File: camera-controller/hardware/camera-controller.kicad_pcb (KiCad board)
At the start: 4 copper layers, 40 x 40 mm, 69 parts, among them J2 Conn_Coaxial, J3 Conn_01x04, J4 Conn_01x08, J5 Micro_SD_Card_Det1, J6 Conn_01x02, U1 STM32H523RCTx, U2 LR2021, Y1 32.768MHz, Y2 24MHz, Y3 32MHz 10pF

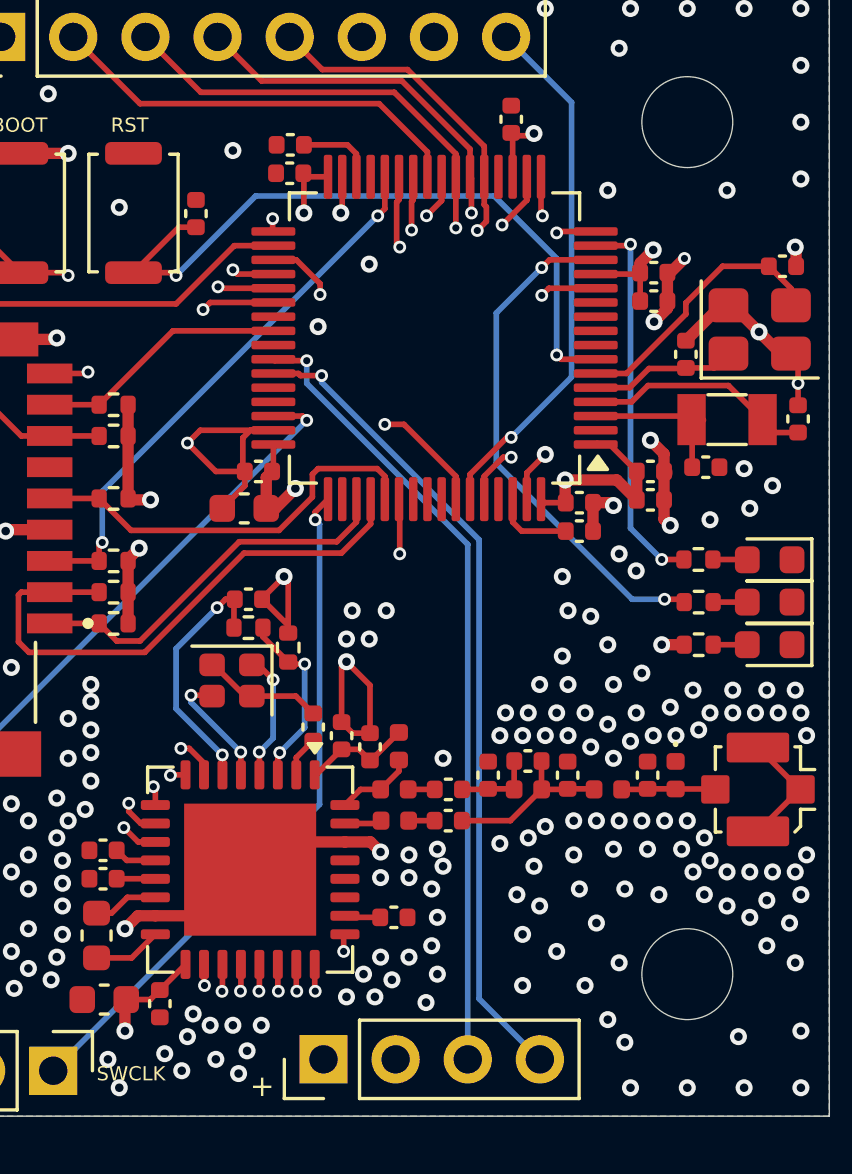
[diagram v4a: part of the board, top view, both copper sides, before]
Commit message: optimized power trace
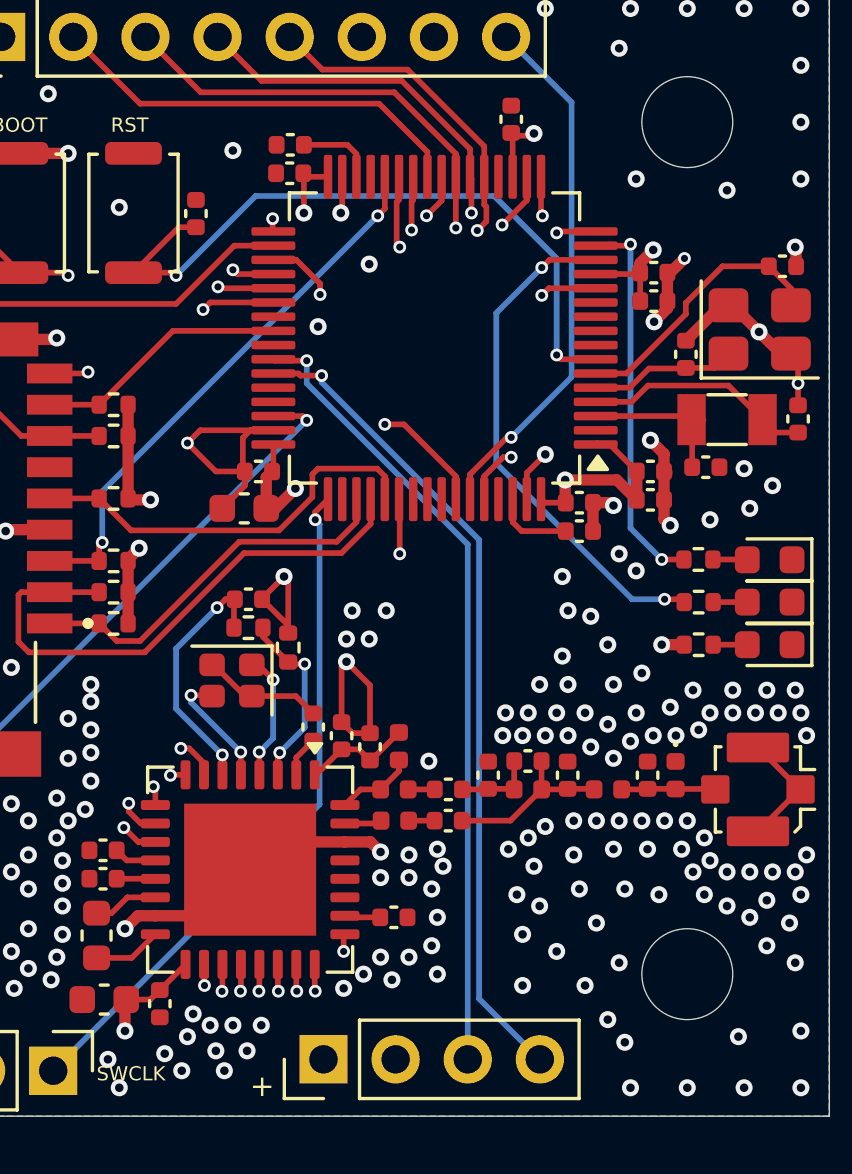
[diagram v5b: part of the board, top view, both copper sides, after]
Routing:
- net +3.3V: track 44.6 -> 69.9 mm
- net GND: vias 232 -> 230
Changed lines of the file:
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@@
 	)
 	(segment
-		(start 125.2 107.38995)
-		(end 127.01005 109.2)
-		(width 0.4)
+		(start 137.7 90.6)
+		(end 140.7 87.6)
+		(width 0.6)
 		(layer "In1.Cu")
 		(net "+3.3V")
 	)
 	(segment
-		(start 130.99 109.2)
-		(end 127.01005 109.2)
-		(width 0.4)
+		(start 125.4 107.731371)
+		(end 125.4 107.2)
+		(width 0.6)
 		(layer "In1.Cu")
 		(net "+3.3V")
 	)
 	(segment
-		(start 125.2 107)
-		(end 125.2 107.38995)
-		(width 0.4)
+		(start 132.19 108)
+		(end 132.19 107.91)
+		(width 0.6)
 		(layer "In1.Cu")
 		(net "+3.3V")
 	)
 	(segment
+		(start 130.99 109.2)
+		(end 126.868629 109.2)
+		(width 0.6)
+		(layer "In1.Cu")
+		(net "+3.3V")
+	)
+	(segment
 		(start 132.19 108)
 		(end 130.99 109.2)
-		(width 0.4)
+		(width 0.6)
+		(layer "In1.Cu")
+		(net "+3.3V")
+	)
+	(segment
+		(start 135.831371 106.5)
+		(end 137.7 104.631371)
+		(width 0.6)
+		(layer "In1.Cu")
+		(net "+3.3V")
+	)
+	(segment
+		(start 132.19 108)
+		(end 132.2 108)
+		(width 0.6)
+		(layer "In1.Cu")
+		(net "+3.3V")
+	)
+	(segment
+		(start 133.7 106.5)
+		(end 135.831371 106.5)
+		(width 0.6)
+		(layer "In1.Cu")
+		(net "+3.3V")
+	)
+	(segment
+		(start 126.868629 109.2)
+		(end 125.4 107.731371)
+		(width 0.6)
+		(layer "In1.Cu")
+		(net "+3.3V")
+	)
+	(segment
+		(start 137.7 104.631371)
+		(end 137.7 90.6)
+		(width 0.6)
+		(layer "In1.Cu")
+		(net "+3.3V")
+	)
+	(segment
+		(start 132.2 108)
+		(end 133.7 106.5)
+		(width 0.6)
+		(layer "In1.Cu")
+		(net "+3.3V")
+	)
+	(segment
+		(start 125.4 107.2)
+		(end 125.2 107)
+		(width 0.6)
 		(layer "In1.Cu")
 		(net "+3.3V")
@@
 	)
 	(via
-		(at 129.2 108.5)
+		(at 128.7 108.4)
 		(size 0.6)
 		(drill 0.3)
@@
 	)
 	(via
-		(at 138.4 100.4)
+		(at 138.7 100.6)
 		(size 0.6)
 		(drill 0.3)
@@
 	)
 	(via
-		(at 128.4 108)
+		(at 128.4 107.7)
 		(size 0.6)
 		(drill 0.3)
@@
 	(via
 		(at 117 71)
-		(size 0.6)
-		(drill 0.3)
-		(layers "F.Cu" "B.Cu")
-		(free yes)
-		(net "GND")
-	)
-	(via
-		(at 134 105.8)
 		(size 0.6)
 		(drill 0.3)
@@
 	)
 	(via
-		(at 138.4 96.6)
+		(at 138.5 96.6)
 		(size 0.6)
 		(drill 0.3)
@@
 	)
 	(via
-		(at 142.2 77.4)
+		(at 143.2 77)
 		(size 0.6)
 		(drill 0.3)
@@
 	)
 	(via
-		(at 136.4 97.4)
+		(at 135.9 97.5)
 		(size 0.6)
 		(drill 0.3)
@@
 	)
 	(via
-		(at 135.8 106)
-		(size 0.6)
-		(drill 0.3)
-		(layers "F.Cu" "B.Cu")
-		(free yes)
-		(net "GND")
-	)
-	(via
 		(at 139.2 96.6)
 		(size 0.6)
@@
 	)
 	(via
-		(at 133 105.8)
-		(size 0.6)
-		(drill 0.3)
+		(at 132.9 105.5)
+		(size 0.6)
+		(drill 0.3)
